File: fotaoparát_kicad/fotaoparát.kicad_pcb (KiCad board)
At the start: 4 copper layers, 34 parts, among them J1 Conn_01x01_Pin, J10 Conn_01x01_Pin, J11 Conn_01x01_Pin, J12 Conn_01x01_Pin, J2 Conn_01x01_Pin, J3 Conn_01x01_Pin, J4 Conn_01x01_Pin, J5 Conn_01x01_Pin, J6 Conn_01x01_Pin, J7 Conn_01x01_Pin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

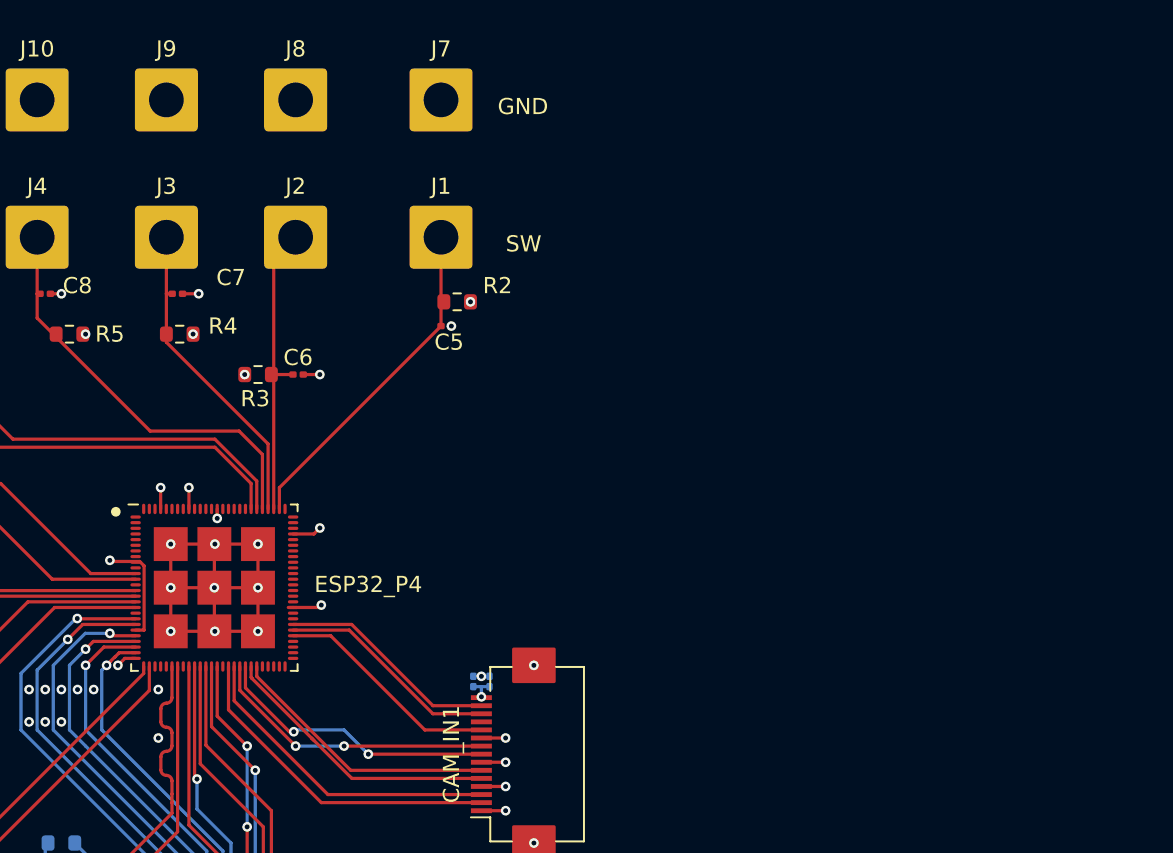
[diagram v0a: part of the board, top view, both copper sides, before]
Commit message: Udelani USB-C konektoru, reset a flash tlacitek
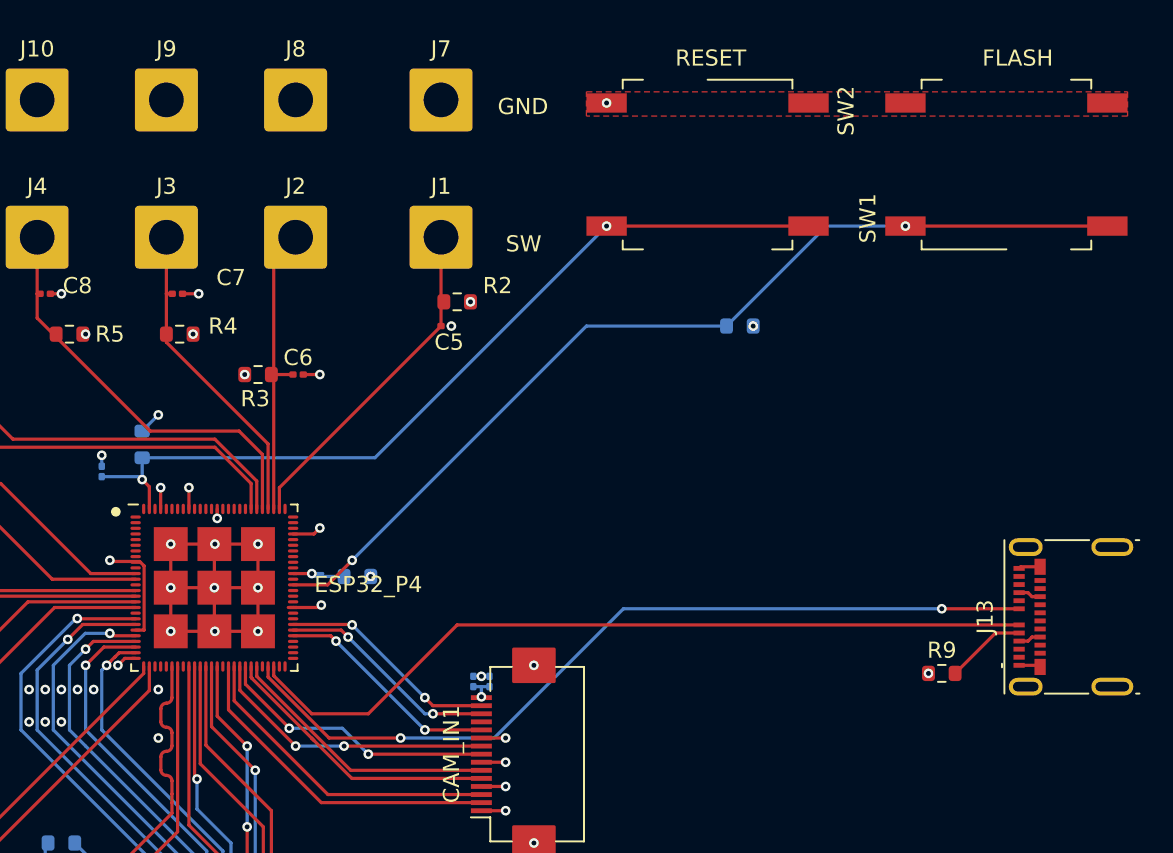
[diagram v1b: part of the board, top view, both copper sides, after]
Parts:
- added C11: 100nF, Capacitor_SMD:C_0201_0603Metric, B.Cu at (149.5, 76.5)
- added J13: USB_C_Receptacle, Connector_USB:USB_C_Receptacle_Molex_105450-0101, F.Cu at (209.5, 85.5)
- added R10: 10k, Resistor_SMD:R_0603_1608Metric, B.Cu at (165.3, 83.0)
- added R11: 10k, Resistor_SMD:R_0603_1608Metric, B.Cu at (152.0, 74.8)
- added R12: 10k, Resistor_SMD:R_0603_1608Metric, B.Cu at (189.0, 67.5)
- added R9: 5k1, Resistor_SMD:R_0603_1608Metric, F.Cu at (201.5, 89.0)
- added SW1: SW_MEC_5G, Button_Switch_SMD:SW_MEC_5GSH9, F.Cu at (205.5, 57.5)
- added SW2: SW_MEC_5G, Button_Switch_SMD:SW_MEC_5GSH9, F.Cu at (187.0, 57.5)
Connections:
- ESP32_P4 pad 102: unconnected-(ESP32_P4-VDD_BAT-Pad102) -> +3.3V
- ESP32_P4 pad 103: unconnected-(ESP32_P4-CHIP_PU-Pad103) -> Net-(ESP32_P4-CHIP_PU)
- ESP32_P4 pad 49: unconnected-(ESP32_P4-USB-DM-Pad49) -> Net-(ESP32_P4-USB-DM)
- ESP32_P4 pad 50: unconnected-(ESP32_P4-USB-DP-Pad50) -> Net-(ESP32_P4-USB-DP)
- ESP32_P4 pad 66: unconnected-(ESP32_P4-GPIO35-Pad66) -> Net-(ESP32_P4-GPIO35)
- ESP32_P4 pad 68: unconnected-(ESP32_P4-GPIO36-Pad68) -> Net-(ESP32_P4-GPIO36)
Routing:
- net Net-(ESP32_P4-GPIO35): track 0.00 -> 59.4 mm, vias 0 -> 2
- net Net-(ESP32_P4-CHIP_PU): track 0.00 -> 53.1 mm, vias 0 -> 2
- net Net-(ESP32_P4-USB-DM): track 0.00 -> 52.0 mm, vias 0 -> 2
- net Net-(ESP32_P4-USB-DP): track 0.00 -> 50.0 mm
- net Net-(J13-CC1): track 0.00 -> 5.00 mm
- net Net-(ESP32_P4-GPIO36): track 0.00 -> 3.91 mm, vias 0 -> 1
- net GND: track 51.2 -> 54.4 mm, vias 44 -> 47
- net Net-(J13-VBUS-PadA4): track 0.00 -> 2.81 mm
- net +3.3V: track 24.9 -> 26.4 mm, vias 17 -> 20
- net Net-(CAM_IN1-Pin_14): vias 0 -> 2
- net Net-(CAM_IN1-Pin_11): vias 0 -> 2
- net Net-(CAM_IN1-Pin_13): vias 0 -> 2
- added copper zone on F.Cu, net GND
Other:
- board text added: "FLASH"
- board text added: "RESET"

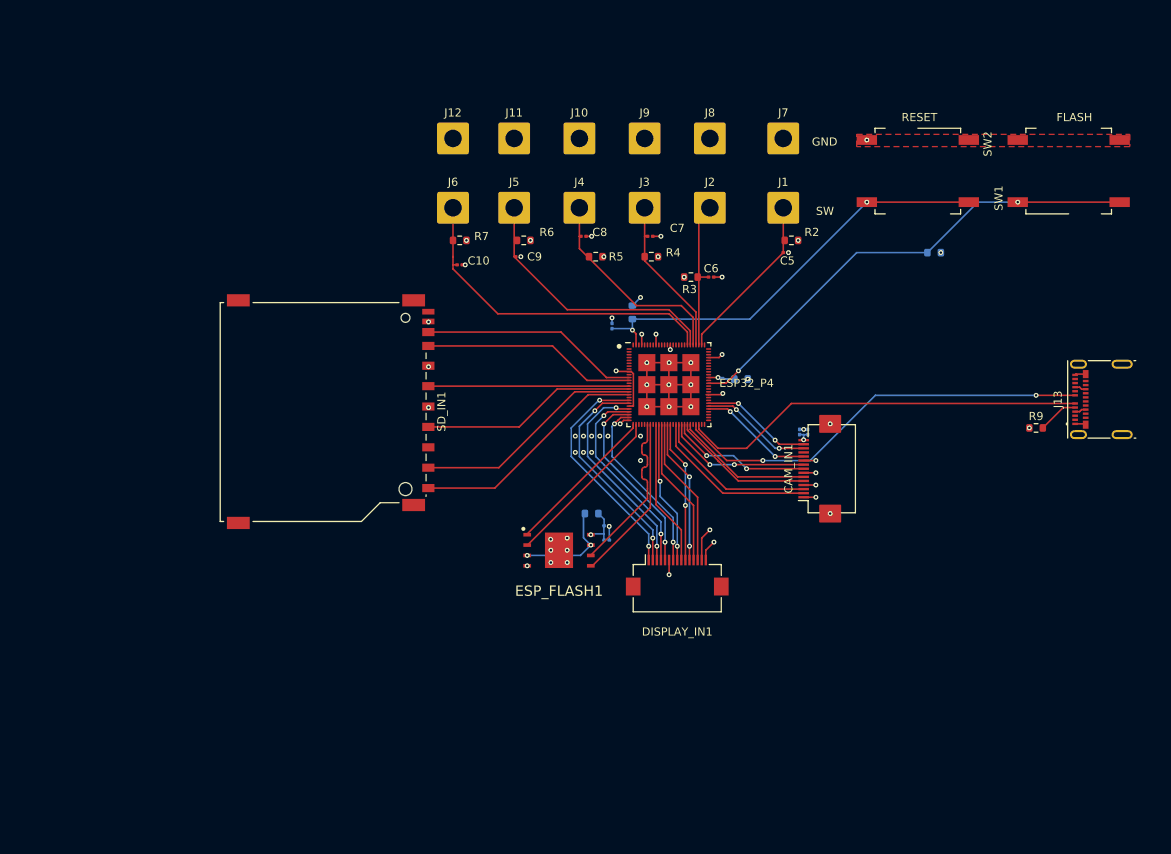
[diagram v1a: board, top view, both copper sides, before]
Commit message: Delal jsem znova flash, predelal jsem usb-c konektor a display konektor
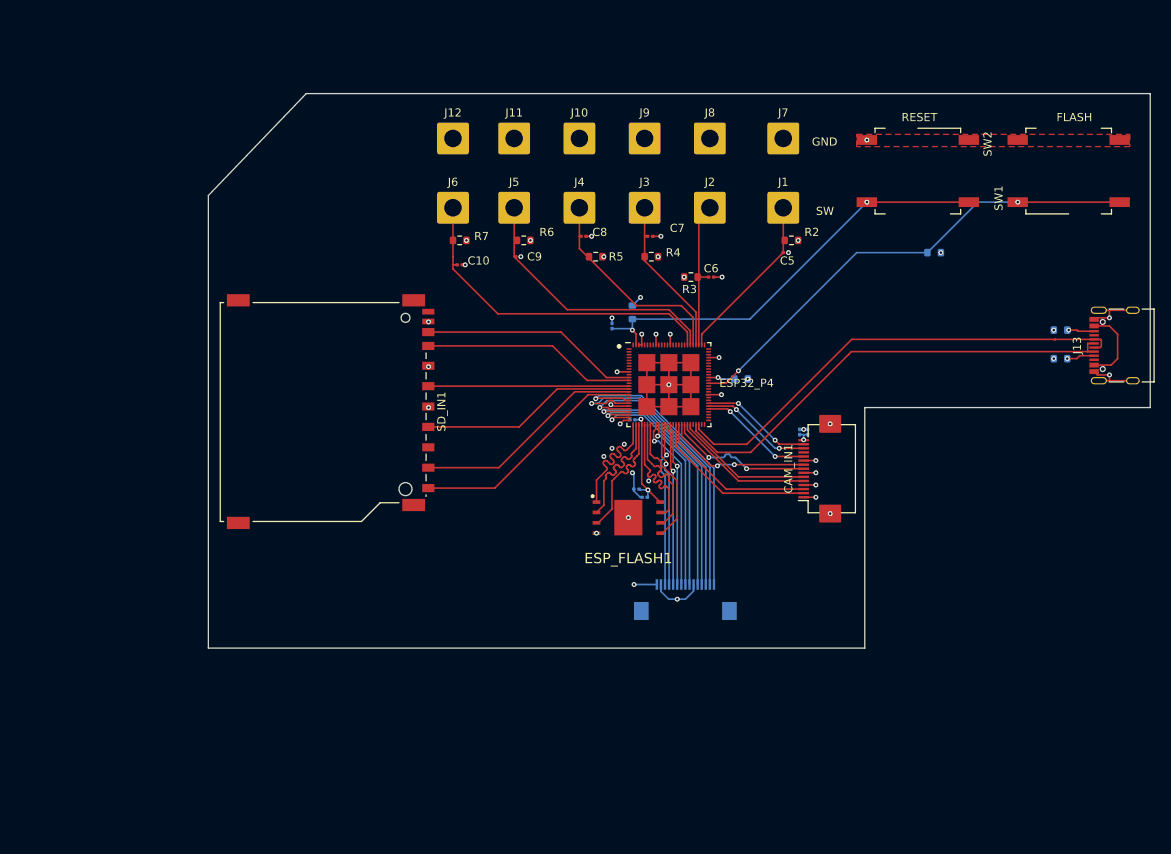
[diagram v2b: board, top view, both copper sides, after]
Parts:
- added C12: 1uF, Capacitor_SMD:C_0201_0603Metric, B.Cu at (153.5, 97.5)
- C1: value 100nF -> 0,1uF
- C2: value 1uF -> 0,1uF
- DISPLAY_IN1, R9: moved to B.Cu
- J13: value USB_C_Receptacle -> USB_C_Receptacle_USB2.0_16P; footprint Connector_USB:USB_C_Receptacle_Molex_105450-0101 -> Connector_USB:USB_C_Receptacle_Palconn_UTC16-G
- R1: value 10k -> 5k1
- moved R1 60.6 mm to (204.5, 80.5), turned to 0 degrees
- moved C1 15.1 mm to (152.0, 88.0)
- moved R9 12.4 mm to (204.5, 77.0)
- moved ESP_FLASH1 9.39 mm to (151.5, 100.0)
- moved J13 6.81 mm to (211.1, 78.9)
- moved C2 5.80 mm to (152.5, 96.5)
- moved DISPLAY_IN1 3.16 mm to (158.5, 110.0), turned to 180 degrees
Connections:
- net /FLASH_(IO1)_1 renamed /FLASH_DO_IO_(IO1)_1
- C1 pad 1: +3.3V -> GND
- C1 pad 2: GND -> /FLASH_VCC
- C2 pad 1: +3.3V -> GND
- C2 pad 2: GND -> /FLASH_VCC
- ESP32_P4 pad 29: unconnected-(ESP32_P4-FLASH_WP-Pad29) -> /FLASH_DO_IO_(IO1)_2
- ESP32_P4 pad 30: unconnected-(ESP32_P4-VDD_FLASH_IO-Pad30) -> /FLASH_VCC
- ESP32_P4 pad 31: unconnected-(ESP32_P4-FLASH_HOLD-Pad31) -> /FLASH_IO3
- ESP_FLASH1 pad 3: /FLASH_DO_(IO1)_2 -> /FLASH_DO_IO_(IO1)_2
- ESP_FLASH1 pad 7: /FLASH_DO_(IO1)_2 -> /FLASH_IO3
- ESP_FLASH1 pad 8: +3.3V -> /FLASH_VCC
- J13 pad B5: unconnected-(J13-CC2-PadB5) -> Net-(J13-CC2)
- J13 pad B6: unconnected-(J13-D+-PadB6) -> Net-(ESP32_P4-USB-DP)
- J13 pad B7: unconnected-(J13-D--PadB7) -> Net-(ESP32_P4-USB-DM)
- R1 pad 1: +3.3V -> GND
- R1 pad 2: /FLASH_DO_(IO1)_2 -> Net-(J13-CC1)
- R9 pad 2: Net-(J13-CC1) -> Net-(J13-CC2)
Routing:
- net /FLASH_DO_IO_(IO1)_2: track 0.00 -> 16.0 mm
- net /FLASH_IO3: track 0.00 -> 15.9 mm
- net /FLASH_VCC: track 0.00 -> 14.3 mm, vias 0 -> 2
- net GND: track 54.4 -> 68.1 mm, vias 47 -> 30
- net /FLASH_DO_(IO1)_2: track 12.6 -> 0.00 mm, vias 2 -> 0
- net /RST: track 27.4 -> 37.5 mm, vias 2 -> 1
- net /I2C_SDA: track 26.2 -> 34.8 mm, vias 2 -> 1
- net /DEBUG: track 28.6 -> 36.8 mm, vias 2 -> 1
- net Net-(ESP32_P4-USB-DP): track 50.0 -> 57.9 mm
- net /INT: track 24.7 -> 32.5 mm, vias 2 -> 1
- net /I2C_SCL: track 23.4 -> 31.1 mm, vias 2 -> 1
- net +3.3V: track 26.4 -> 18.7 mm
- net /LED_PWM: track 22.1 -> 29.4 mm, vias 2 -> 1
- net Net-(J13-VBUS-PadA4): track 2.81 -> 9.52 mm
- net Net-(ESP32_P4-USB-DM): track 52.0 -> 57.6 mm, vias 2 -> 0
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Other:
- board outline added: 115.5 x 68 mm

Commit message: nejake nesrovnalosti
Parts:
- added SvVít design: LOGO, LOGO, F.Cu at (113.5, 59.5)

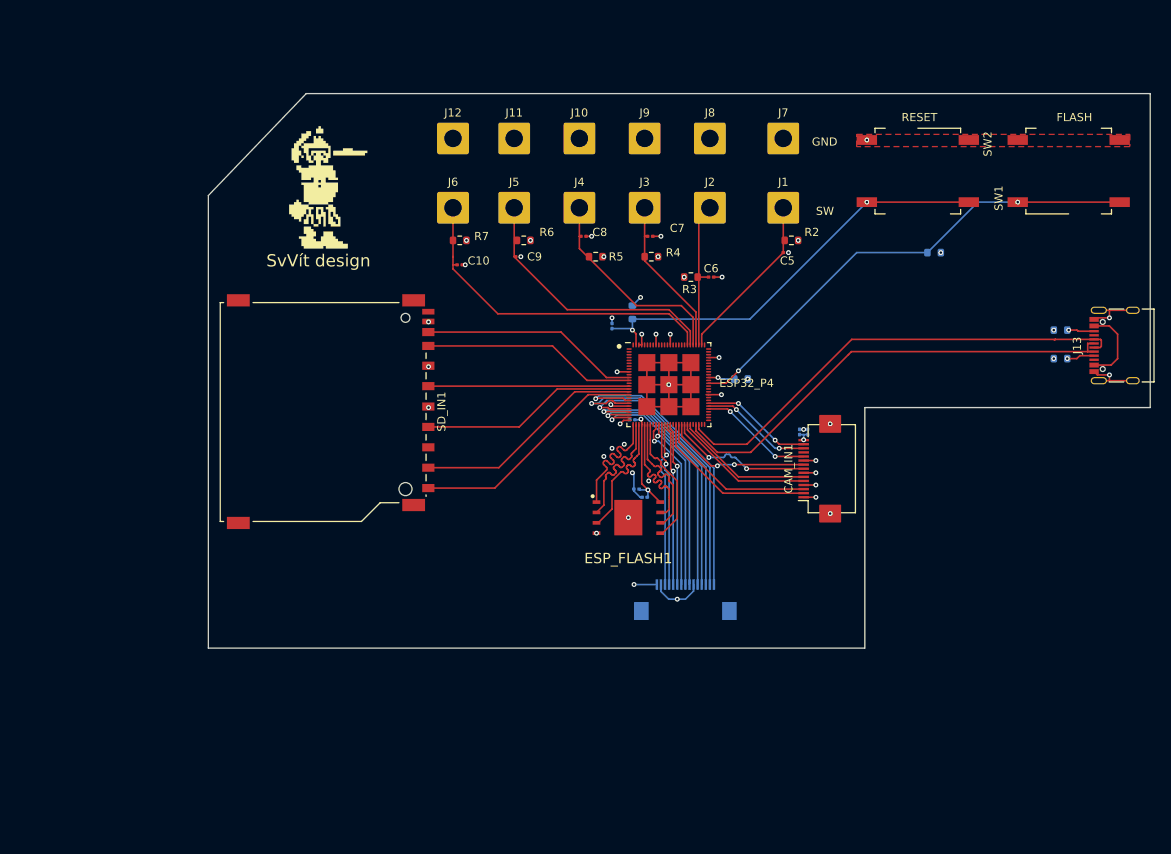
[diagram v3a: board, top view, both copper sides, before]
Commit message: optimalizace routingu, oprava chyb, pridani baterky do soupisu mimo pcb
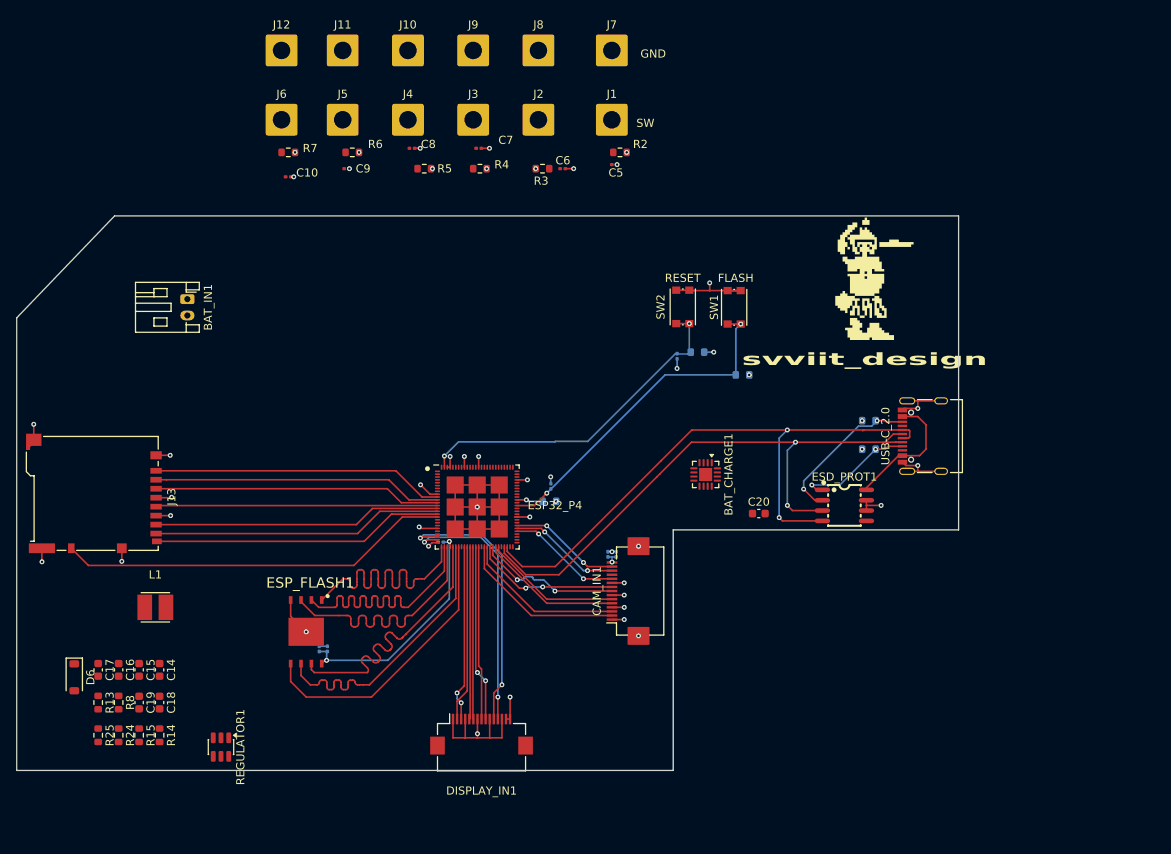
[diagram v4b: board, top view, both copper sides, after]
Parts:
- removed SD_IN1: Micro_SD_Card_Det1, Connector_Card:SD_TE_2041021
- added BAT_CHARGE1: BQ24073RGT, Package_DFN_QFN:VQFN-16-1EP_3x3mm_P0.5mm_EP1.6x1.6mm, F.Cu at (161.0, 94.7)
- added BAT_IN1: Conn_01x02_Socket, Connector_JST:JST_PH_S2B-PH-K_1x02_P2.00mm_Horizontal, F.Cu at (97.4, 73.2)
- added C13: 100nF, Capacitor_SMD:C_0201_0603Metric, B.Cu at (142.0, 96.2)
- added C14: 10uF, Capacitor_SMD:C_0603_1608Metric, F.Cu at (94.0, 118.7)
- added C15: 100n, Capacitor_SMD:C_0603_1608Metric, F.Cu at (91.5, 118.7)
- added C16: 22uF, Capacitor_SMD:C_0603_1608Metric, F.Cu at (89.0, 118.7)
- added C17: 100n, Capacitor_SMD:C_0603_1608Metric, F.Cu at (86.5, 118.7)
- added C18: 1u, Capacitor_SMD:C_0603_1608Metric, F.Cu at (94.0, 122.7)
- added C19: 22uF, Capacitor_SMD:C_0603_1608Metric, F.Cu at (91.5, 122.7)
- added C20: 1u, Capacitor_SMD:C_0603_1608Metric, F.Cu at (167.5, 99.5)
- added D6: 3v6 Zener, Diode_SMD:D_SOD-123, F.Cu at (83.6, 119.6)
- added ESD_PROT1: ESDA6V1U1RL, stlib:SO-8_L4.9-W3.9-P1.27-LS5.9-BL, F.Cu at (178.0, 98.5)
- added J13: Micro_SD_Card_Det2, Connector_Card:microSD_HC_Hirose_DM3BT-DSF-PEJS, F.Cu at (86.0, 97.0)
- added L1: 4,7uH, stlib:IND-SMD_L3.5-W3.0, F.Cu at (93.5, 111.0)
- added R13: 620, Resistor_SMD:R_0603_1608Metric, F.Cu at (86.5, 122.7)
- added R14: 10k, Resistor_SMD:R_0603_1608Metric, F.Cu at (94.0, 126.7)
- added R15: 1k1, Resistor_SMD:R_0603_1608Metric, F.Cu at (91.5, 126.7)
- added R24: 10k, Resistor_SMD:R_0603_1608Metric, F.Cu at (89.0, 126.7)
- added R25: 10k, Resistor_SMD:R_0603_1608Metric, F.Cu at (86.5, 126.7)
- added R8: 10k, Resistor_SMD:R_0603_1608Metric, F.Cu at (89.0, 122.7)
- added REGULATOR1: AP63203WU, Package_TO_SOT_SMD:TSOT-23-6, F.Cu at (101.5, 128.1)
- DISPLAY_IN1: moved to F.Cu
- SW1, SW2: footprint Button_Switch_SMD:SW_MEC_5GSH9 -> Button_Switch_SMD:SW_Push_1P1T_NO_CK_KMR2
- svviit_design: renamed from SvVít design
- moved svviit_design 67.9 mm to (180.5, 70.7)
- moved SW1 44.3 mm to (164.5, 74.2)
- moved C12 44.0 mm to (113.6, 116.1), turned to -90 degrees
- moved C2 42.7 mm to (114.6, 116.1), turned to -90 degrees
- moved ESP_FLASH1 41.9 mm to (112.0, 114.0), turned to -90 degrees
- moved SW2 33.3 mm to (158.2, 74.2)
- moved DISPLAY_IN1 30.0 mm to (133.5, 126.5), turned to 0 degrees
- moved C1 27.9 mm to (128.5, 103.0)
- moved C3 27.9 mm to (150.0, 104.5)
- moved C4 27.9 mm to (149.0, 104.5)
- moved CAM_IN1 27.9 mm to (151.3, 109.0)
- moved ESP32_P4 27.9 mm to (133.0, 98.7)
- moved R10 27.9 mm to (141.8, 98.0)
- moved R12 27.9 mm to (165.5, 82.5)
- moved R1 26.0 mm to (181.0, 91.6)
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- renumbered J13 to USB-C_2.0
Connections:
- net Net-(J13-VBUS-PadA4) renamed +5V
- DISPLAY_IN1 pad 1: /DEBUG -> GND
- DISPLAY_IN1 pad 10: /DSI_DATAN0 -> GND
- DISPLAY_IN1 pad 11: /DSI_DATAP0 -> /I2C_SCL
- DISPLAY_IN1 pad 12: /DSI_CLKN -> /I2C_SDA
- DISPLAY_IN1 pad 13: /DSI_CLKP -> GND
- DISPLAY_IN1 pad 14: GND -> +3V3
- DISPLAY_IN1 pad 15: +3.3V -> +3V3
- DISPLAY_IN1 pad 2: /RST -> /DSI_DATAN1
- DISPLAY_IN1 pad 3: /I2C_SDA -> /DSI_DATAP1
- DISPLAY_IN1 pad 4: /INT -> GND
- DISPLAY_IN1 pad 5: /I2C_SCL -> /DSI_CLKN
- DISPLAY_IN1 pad 6: GND -> /DSI_CLKP
- DISPLAY_IN1 pad 7: /LED_PWM -> unconnected-(DISPLAY_IN1-Pin_7-Pad7)
- DISPLAY_IN1 pad 8: /DSI_DATAN1 -> /DSI_DATAN0
- DISPLAY_IN1 pad 9: /DSI_DATAP1 -> /DSI_DATAP0
- ESP32_P4 pad 1: unconnected-(ESP32_P4-GPIO1/ADC-Pad1) -> /A3
- ESP32_P4 pad 10: unconnected-(ESP32_P4-GPIO9/ADC-Pad10) -> /DAT2
- ESP32_P4 pad 11: /DAT1 -> /DAT3/CD
- ESP32_P4 pad 12: /DAT0 -> /CMD
- ESP32_P4 pad 13: unconnected-(ESP32_P4-GPIO12/ADC-Pad13) -> /CLK
- ESP32_P4 pad 14: /CLK -> /DAT0
- ESP32_P4 pad 15: /CMD -> /DAT1
- ESP32_P4 pad 16: /DAT2 -> /DET2
- ESP32_P4 pad 17: /DET -> /DET1
- ESP32_P4 pad 19: /DEBUG -> unconnected-(ESP32_P4-GPIO18/ADC-Pad19)
- ESP32_P4 pad 2: unconnected-(ESP32_P4-GPIO2/ADC-Pad2) -> /BATT_CHG
- ESP32_P4 pad 20: /RST -> unconnected-(ESP32_P4-GPIO19/ADC-Pad20)
- ESP32_P4 pad 22: /I2C_SDA -> unconnected-(ESP32_P4-GPIO20/ADC-Pad22)
- ESP32_P4 pad 23: /INT -> unconnected-(ESP32_P4-GPIO21/ADC-Pad23)
- ESP32_P4 pad 25: /LED_PWM -> /I2C_SDA
- ESP32_P4 pad 3: unconnected-(ESP32_P4-GPIO3/ADC-Pad3) -> /BATT_PG
- SW1 pad 1: Net-(ESP32_P4-GPIO35) -> GND
- SW1 pad 2: Net-(ESP32_P4-GPIO35) -> GND
- SW2 pad 1: GND -> Net-(ESP32_P4-CHIP_PU)
- SW2 pad 2: GND -> Net-(ESP32_P4-CHIP_PU)
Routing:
- net /DET1: track 0.00 -> 48.2 mm
- net Net-(ESP32_P4-VDD_IO_5): track 41.5 -> 0.00 mm
- net GND: track 68.1 -> 107.2 mm, vias 30 -> 29
- net /RST: track 37.5 -> 0.00 mm, vias 1 -> 0
- net /DEBUG: track 36.8 -> 0.00 mm, vias 1 -> 0
- net /DET2: track 0.00 -> 35.8 mm
- net /DAT3/CD: track 0.00 -> 35.5 mm
- net Net-(ESP32_P4-GPIO43): track 33.1 -> 0.00 mm
- net /INT: track 32.5 -> 0.00 mm, vias 1 -> 0
- net /LED_PWM: track 29.4 -> 0.00 mm, vias 1 -> 0
- net /DET: track 29.4 -> 0.00 mm
- net Net-(ESP32_P4-GPIO42): track 26.0 -> 0.00 mm
- net Net-(ESP32_P4-GPIO39): track 21.0 -> 0.00 mm
- net Net-(ESP32_P4-GPIO41): track 19.8 -> 0.00 mm
- net /FLASH_DI_(IO0): track 16.0 -> 35.5 mm
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- removed copper zone on F.Cu, net GND
